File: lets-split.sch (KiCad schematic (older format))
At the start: 54 parts, among them J1 USB_C_Receptacle_USB2.0, SW1 Key_Tab, SW10 Key_D, SW11 Key_F, SW12 Key_G, SW13 Key_Shift, SW14 Key_Z, SW15 Key_X, SW16 Key_C, SW17 Key_V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

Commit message: Corrected footprint associations
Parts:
- D1, D10, D11, D12, D13, D14, D15, D16, D17, D18, D19, D2, D20, D21, D22, D23, D24, D3, D4, D5, D6, D7, D8, D9: footprint Diode_THT:D_DO-34_SOD68_P7.62mm_Horizontal -> Diode_THT:D_DO-35_SOD27_P7.62mm_Horizontal
- R1, R2, R3: footprint Resistor_THT:R_Axial_DIN0207_L6.3mm_D2.5mm_P10.16mm_Horizontal -> Resistor_THT:R_Axial_DIN0207_L6.3mm_D2.5mm_P7.62mm_Horizontal
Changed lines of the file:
@@
 F 0 "D1" V 1546 2070 50  0000 L CNN
 F 1 "D_Small" V 1455 2070 50  0000 L CNN
-F 2 "Diode_THT:D_DO-34_SOD68_P7.62mm_Horizontal" V 1500 2000 50  0001 C CNN
+F 2 "Diode_THT:D_DO-35_SOD27_P7.62mm_Horizontal" V 1500 2000 50  0001 C CNN
 F 3 "~" V 1500 2000 50  0001 C CNN
 	1    1500 2000
@@
 F 0 "D2" V 2346 2070 50  0000 L CNN
 F 1 "D_Small" V 2255 2070 50  0000 L CNN
-F 2 "Diode_THT:D_DO-34_SOD68_P7.62mm_Horizontal" V 2300 2000 50  0001 C CNN
+F 2 "Diode_THT:D_DO-35_SOD27_P7.62mm_Horizontal" V 2300 2000 50  0001 C CNN
 F 3 "~" V 2300 2000 50  0001 C CNN
 	1    2300 2000
@@
 F 0 "D3" V 3196 2070 50  0000 L CNN
 F 1 "D_Small" V 3105 2070 50  0000 L CNN
-F 2 "Diode_THT:D_DO-34_SOD68_P7.62mm_Horizontal" V 3150 2000 50  0001 C CNN
+F 2 "Diode_THT:D_DO-35_SOD27_P7.62mm_Horizontal" V 3150 2000 50  0001 C CNN
 F 3 "~" V 3150 2000 50  0001 C CNN
 	1    3150 2000
@@
 F 0 "D4" V 4046 2070 50  0000 L CNN
 F 1 "D_Small" V 3955 2070 50  0000 L CNN
-F 2 "Diode_THT:D_DO-34_SOD68_P7.62mm_Horizontal" V 4000 2000 50  0001 C CNN
+F 2 "Diode_THT:D_DO-35_SOD27_P7.62mm_Horizontal" V 4000 2000 50  0001 C CNN
 F 3 "~" V 4000 2000 50  0001 C CNN
 	1    4000 2000
@@
 F 0 "D5" V 4846 2070 50  0000 L CNN
 F 1 "D_Small" V 4755 2070 50  0000 L CNN
-F 2 "Diode_THT:D_DO-34_SOD68_P7.62mm_Horizontal" V 4800 2000 50  0001 C CNN
+F 2 "Diode_THT:D_DO-35_SOD27_P7.62mm_Horizontal" V 4800 2000 50  0001 C CNN
 F 3 "~" V 4800 2000 50  0001 C CNN
 	1    4800 2000
@@
 F 0 "D6" V 5746 2070 50  0000 L CNN
 F 1 "D_Small" V 5655 2070 50  0000 L CNN
-F 2 "Diode_THT:D_DO-34_SOD68_P7.62mm_Horizontal" V 5700 2000 50  0001 C CNN
+F 2 "Diode_THT:D_DO-35_SOD27_P7.62mm_Horizontal" V 5700 2000 50  0001 C CNN
 F 3 "~" V 5700 2000 50  0001 C CNN
 	1    5700 2000
@@
 F 0 "D7" V 1546 2670 50  0000 L CNN
 F 1 "D_Small" V 1455 2670 50  0000 L CNN
-F 2 "Diode_THT:D_DO-34_SOD68_P7.62mm_Horizontal" V 1500 2600 50  0001 C CNN
+F 2 "Diode_THT:D_DO-35_SOD27_P7.62mm_Horizontal" V 1500 2600 50  0001 C CNN
 F 3 "~" V 1500 2600 50  0001 C CNN
 	1    1500 2600
@@
 F 0 "D8" V 2346 2670 50  0000 L CNN
 F 1 "D_Small" V 2255 2670 50  0000 L CNN
-F 2 "Diode_THT:D_DO-34_SOD68_P7.62mm_Horizontal" V 2300 2600 50  0001 C CNN
+F 2 "Diode_THT:D_DO-35_SOD27_P7.62mm_Horizontal" V 2300 2600 50  0001 C CNN
 F 3 "~" V 2300 2600 50  0001 C CNN
 	1    2300 2600
@@
 F 0 "D9" V 3196 2670 50  0000 L CNN
 F 1 "D_Small" V 3105 2670 50  0000 L CNN
-F 2 "Diode_THT:D_DO-34_SOD68_P7.62mm_Horizontal" V 3150 2600 50  0001 C CNN
+F 2 "Diode_THT:D_DO-35_SOD27_P7.62mm_Horizontal" V 3150 2600 50  0001 C CNN
 F 3 "~" V 3150 2600 50  0001 C CNN
 	1    3150 2600
@@
 F 0 "D10" V 4046 2670 50  0000 L CNN
 F 1 "D_Small" V 3955 2670 50  0000 L CNN
-F 2 "Diode_THT:D_DO-34_SOD68_P7.62mm_Horizontal" V 4000 2600 50  0001 C CNN
+F 2 "Diode_THT:D_DO-35_SOD27_P7.62mm_Horizontal" V 4000 2600 50  0001 C CNN
 F 3 "~" V 4000 2600 50  0001 C CNN
 	1    4000 2600
@@
 F 0 "D11" V 4846 2670 50  0000 L CNN
 F 1 "D_Small" V 4755 2670 50  0000 L CNN
-F 2 "Diode_THT:D_DO-34_SOD68_P7.62mm_Horizontal" V 4800 2600 50  0001 C CNN
+F 2 "Diode_THT:D_DO-35_SOD27_P7.62mm_Horizontal" V 4800 2600 50  0001 C CNN
 F 3 "~" V 4800 2600 50  0001 C CNN
 	1    4800 2600
@@
 F 0 "D12" V 5746 2670 50  0000 L CNN
 F 1 "D_Small" V 5655 2670 50  0000 L CNN
-F 2 "Diode_THT:D_DO-34_SOD68_P7.62mm_Horizontal" V 5700 2600 50  0001 C CNN
+F 2 "Diode_THT:D_DO-35_SOD27_P7.62mm_Horizontal" V 5700 2600 50  0001 C CNN
 F 3 "~" V 5700 2600 50  0001 C CNN
 	1    5700 2600
@@
 F 0 "D13" V 1546 3270 50  0000 L CNN
 F 1 "D_Small" V 1455 3270 50  0000 L CNN
-F 2 "Diode_THT:D_DO-34_SOD68_P7.62mm_Horizontal" V 1500 3200 50  0001 C CNN
+F 2 "Diode_THT:D_DO-35_SOD27_P7.62mm_Horizontal" V 1500 3200 50  0001 C CNN
 F 3 "~" V 1500 3200 50  0001 C CNN
 	1    1500 3200
@@
 F 0 "D14" V 2346 3270 50  0000 L CNN
 F 1 "D_Small" V 2255 3270 50  0000 L CNN
-F 2 "Diode_THT:D_DO-34_SOD68_P7.62mm_Horizontal" V 2300 3200 50  0001 C CNN
+F 2 "Diode_THT:D_DO-35_SOD27_P7.62mm_Horizontal" V 2300 3200 50  0001 C CNN
 F 3 "~" V 2300 3200 50  0001 C CNN
 	1    2300 3200
@@
 F 0 "D15" V 3196 3270 50  0000 L CNN
 F 1 "D_Small" V 3105 3270 50  0000 L CNN
-F 2 "Diode_THT:D_DO-34_SOD68_P7.62mm_Horizontal" V 3150 3200 50  0001 C CNN
+F 2 "Diode_THT:D_DO-35_SOD27_P7.62mm_Horizontal" V 3150 3200 50  0001 C CNN
 F 3 "~" V 3150 3200 50  0001 C CNN
 	1    3150 3200
@@
 F 0 "D16" V 4046 3270 50  0000 L CNN
 F 1 "D_Small" V 3955 3270 50  0000 L CNN
-F 2 "Diode_THT:D_DO-34_SOD68_P7.62mm_Horizontal" V 4000 3200 50  0001 C CNN
+F 2 "Diode_THT:D_DO-35_SOD27_P7.62mm_Horizontal" V 4000 3200 50  0001 C CNN
 F 3 "~" V 4000 3200 50  0001 C CNN
 	1    4000 3200
@@
 F 0 "D17" V 4846 3270 50  0000 L CNN
 F 1 "D_Small" V 4755 3270 50  0000 L CNN
-F 2 "Diode_THT:D_DO-34_SOD68_P7.62mm_Horizontal" V 4800 3200 50  0001 C CNN
+F 2 "Diode_THT:D_DO-35_SOD27_P7.62mm_Horizontal" V 4800 3200 50  0001 C CNN
 F 3 "~" V 4800 3200 50  0001 C CNN
 	1    4800 3200
@@
 F 0 "D18" V 5746 3270 50  0000 L CNN
 F 1 "D_Small" V 5655 3270 50  0000 L CNN
-F 2 "Diode_THT:D_DO-34_SOD68_P7.62mm_Horizontal" V 5700 3200 50  0001 C CNN
+F 2 "Diode_THT:D_DO-35_SOD27_P7.62mm_Horizontal" V 5700 3200 50  0001 C CNN
 F 3 "~" V 5700 3200 50  0001 C CNN
 	1    5700 3200
@@
 F 0 "D19" V 1546 3870 50  0000 L CNN
 F 1 "D_Small" V 1455 3870 50  0000 L CNN
-F 2 "Diode_THT:D_DO-34_SOD68_P7.62mm_Horizontal" V 1500 3800 50  0001 C CNN
+F 2 "Diode_THT:D_DO-35_SOD27_P7.62mm_Horizontal" V 1500 3800 50  0001 C CNN
 F 3 "~" V 1500 3800 50  0001 C CNN
 	1    1500 3800
@@
 F 0 "D20" V 2346 3870 50  0000 L CNN
 F 1 "D_Small" V 2255 3870 50  0000 L CNN
-F 2 "Diode_THT:D_DO-34_SOD68_P7.62mm_Horizontal" V 2300 3800 50  0001 C CNN
+F 2 "Diode_THT:D_DO-35_SOD27_P7.62mm_Horizontal" V 2300 3800 50  0001 C CNN
 F 3 "~" V 2300 3800 50  0001 C CNN
 	1    2300 3800
@@
 F 0 "D21" V 3196 3870 50  0000 L CNN
 F 1 "D_Small" V 3105 3870 50  0000 L CNN
-F 2 "Diode_THT:D_DO-34_SOD68_P7.62mm_Horizontal" V 3150 3800 50  0001 C CNN
+F 2 "Diode_THT:D_DO-35_SOD27_P7.62mm_Horizontal" V 3150 3800 50  0001 C CNN
 F 3 "~" V 3150 3800 50  0001 C CNN
 	1    3150 3800
@@
 F 0 "D22" V 4046 3870 50  0000 L CNN
 F 1 "D_Small" V 3955 3870 50  0000 L CNN
-F 2 "Diode_THT:D_DO-34_SOD68_P7.62mm_Horizontal" V 4000 3800 50  0001 C CNN
+F 2 "Diode_THT:D_DO-35_SOD27_P7.62mm_Horizontal" V 4000 3800 50  0001 C CNN
 F 3 "~" V 4000 3800 50  0001 C CNN
 	1    4000 3800
@@
 F 0 "D23" V 4846 3870 50  0000 L CNN
 F 1 "D_Small" V 4755 3870 50  0000 L CNN
-F 2 "Diode_THT:D_DO-34_SOD68_P7.62mm_Horizontal" V 4800 3800 50  0001 C CNN
+F 2 "Diode_THT:D_DO-35_SOD27_P7.62mm_Horizontal" V 4800 3800 50  0001 C CNN
 F 3 "~" V 4800 3800 50  0001 C CNN
 	1    4800 3800
@@
 F 0 "D24" V 5746 3870 50  0000 L CNN
 F 1 "D_Small" V 5655 3870 50  0000 L CNN
-F 2 "Diode_THT:D_DO-34_SOD68_P7.62mm_Horizontal" V 5700 3800 50  0001 C CNN
+F 2 "Diode_THT:D_DO-35_SOD27_P7.62mm_Horizontal" V 5700 3800 50  0001 C CNN
 F 3 "~" V 5700 3800 50  0001 C CNN
 	1    5700 3800
@@
 F 0 "R3" H 8309 5396 50  0000 L CNN
 F 1 "220" H 8309 5305 50  0000 L CNN
-F 2 "Resistor_THT:R_Axial_DIN0207_L6.3mm_D2.5mm_P10.16mm_Horizontal" H 8250 5350 50  0001 C CNN
+F 2 "Resistor_THT:R_Axial_DIN0207_L6.3mm_D2.5mm_P7.62mm_Horizontal" H 8250 5350 50  0001 C CNN
 F 3 "~" H 8250 5350 50  0001 C CNN
 	1    8250 5350
@@
 F 0 "R2" H 9109 2696 50  0000 L CNN
 F 1 "9.1k" H 9109 2605 50  0000 L CNN
-F 2 "Resistor_THT:R_Axial_DIN0207_L6.3mm_D2.5mm_P10.16mm_Horizontal" H 9050 2650 50  0001 C CNN
+F 2 "Resistor_THT:R_Axial_DIN0207_L6.3mm_D2.5mm_P7.62mm_Horizontal" H 9050 2650 50  0001 C CNN
 F 3 "~" H 9050 2650 50  0001 C CNN
 	1    9050 2650
@@
 F 0 "R1" H 9109 2296 50  0000 L CNN
 F 1 "9.1k" H 9109 2205 50  0000 L CNN
-F 2 "Resistor_THT:R_Axial_DIN0207_L6.3mm_D2.5mm_P10.16mm_Horizontal" H 9050 2250 50  0001 C CNN
+F 2 "Resistor_THT:R_Axial_DIN0207_L6.3mm_D2.5mm_P7.62mm_Horizontal" H 9050 2250 50  0001 C CNN
 F 3 "~" H 9050 2250 50  0001 C CNN
 	1    9050 2250

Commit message: corrected reset button footprint
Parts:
- SW25: footprint keyswitches:SW_MX_reversible -> Button_Switch_THT:SW_PUSH_6mm_H4.3mm
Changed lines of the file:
@@
 F 0 "SW25" H 5650 6535 50  0000 C CNN
 F 1 "Reset" H 5650 6444 50  0000 C CNN
-F 2 "keyswitches:SW_MX_reversible" H 5650 6450 50  0001 C CNN
+F 2 "Button_Switch_THT:SW_PUSH_6mm_H4.3mm" H 5650 6450 50  0001 C CNN
 F 3 "~" H 5650 6450 50  0001 C CNN
 	1    5650 6250

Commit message: Fixed USB-C connector not passing inspection.
Added jumper to allow it to be mounted on either side of the board
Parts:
- added JP1: Jack Reversed Jumper, Jumper:SolderJumper-3_P1.3mm_Open_RoundedPad1.0x1.5mm, symbol Jumper:SolderJumper_3_Open
- added JP2: Jack Obversed Jumper, Jumper:SolderJumper-3_P1.3mm_Open_RoundedPad1.0x1.5mm, symbol Jumper:SolderJumper_3_Open
- J1: footprint Connector_USB:USB_C_Receptacle_GCT_USB4085 -> custom-footprints:USB_C_GCT_USB4085
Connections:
- net at J1.A5 (CC1): now also JP1.3 (B)
- net at J1.B5 (CC2): now also JP1.2 (C)
- new net: J1.A8 (SBU1), JP2.2 (C)
- new net: J1.B8 (SBU2), JP2.1 (A)
- new net: JP1.1 (A), JP2.3 (B), R3.1
- no-connect marks 6 -> 11
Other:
- moved on the sheet: R3
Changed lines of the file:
@@
 F 0 "J1" H 8620 4789 50  0000 R CNN
 F 1 "USB_C_Receptacle_USB2.0" H 8620 4698 50  0000 R CNN
-F 2 "Connector_USB:USB_C_Receptacle_GCT_USB4085" H 9200 4850 50  0001 C CNN
+F 2 "custom-footprints:USB_C_GCT_USB4085" H 9200 4850 50  0001 C CNN
 F 3 "https://www.usb.org/sites/default/files/documents/usb_type-c.zip" H 9200 4850 50  0001 C CNN
 	1    9050 4850
@@
 Text GLabel 2150 5950 0    50   Input ~ 0
 Serial1
-Text GLabel 8050 5350 0    50   Input ~ 0
+Text GLabel 7500 4950 0    50   Input ~ 0
 Serial1
-Wire Wire Line
-	8350 5350 8450 5350
-Wire Wire Line
-	8450 5450 8450 5350
-Connection ~ 8450 5350
 $Comp
 L power:VCC #PWR03
@@
 L Device:R_Small R3
 U 1 1 60DE63E5
-P 8250 5350
-F 0 "R3" H 8309 5396 50  0000 L CNN
-F 1 "220" H 8309 5305 50  0000 L CNN
-F 2 "Resistor_THT:R_Axial_DIN0207_L6.3mm_D2.5mm_P7.62mm_Horizontal" H 8250 5350 50  0001 C CNN
-F 3 "~" H 8250 5350 50  0001 C CNN
-	1    8250 5350
+P 7700 4950
+F 0 "R3" H 7759 4996 50  0000 L CNN
+F 1 "220" H 7759 4905 50  0000 L CNN
+F 2 "Resistor_THT:R_Axial_DIN0207_L6.3mm_D2.5mm_P7.62mm_Horizontal" H 7700 4950 50  0001 C CNN
+F 3 "~" H 7700 4950 50  0001 C CNN
+	1    7700 4950
 	0    1    1    0
 $EndComp
-NoConn ~ 8450 4550
-NoConn ~ 8450 4450
 NoConn ~ 8450 4750
 NoConn ~ 8450 4850
@@
 Comms
 Wire Wire Line
-	8050 5350 8150 5350
+	7500 4950 7600 4950
 Wire Wire Line
 	9050 5850 9050 5750
@@
 Text Notes 5200 5550 0    118  ~ 0
 Reset Button
+NoConn ~ 2150 5850
+NoConn ~ 2150 6250
+NoConn ~ 2150 6350
+NoConn ~ 2150 6450
+NoConn ~ 2150 6550
+NoConn ~ 3550 6250
+NoConn ~ 3550 5850
+$Comp
+L Jumper:SolderJumper_3_Open JP1
+U 1 1 60EF25DC
+P 8000 4450
+F 0 "JP1" H 8000 4655 50  0000 C CNN
+F 1 "Jack Reversed Jumper" H 8000 4564 50  0000 C CNN
+F 2 "Jumper:SolderJumper-3_P1.3mm_Open_RoundedPad1.0x1.5mm" H 8000 4450 50  0001 C CNN
+F 3 "~" H 8000 4450 50  0001 C CNN
+	1    8000 4450
+	1    0    0    -1
+$EndComp
+$Comp
+L Jumper:SolderJumper_3_Open JP2
+U 1 1 60EF4046
+P 8000 5450
+F 0 "JP2" H 8000 5563 50  0000 C CNN
+F 1 "Jack Obversed Jumper" H 8000 5654 50  0000 C CNN
+F 2 "Jumper:SolderJumper-3_P1.3mm_Open_RoundedPad1.0x1.5mm" H 8000 5450 50  0001 C CNN
+F 3 "~" H 8000 5450 50  0001 C CNN
+	1    8000 5450
+	-1   0    0    1
+$EndComp
+Wire Wire Line
+	7800 5450 7800 4950
+Wire Wire Line
+	7800 4950 7800 4450
+Connection ~ 7800 4950
+Wire Wire Line
+	8000 4600 8450 4600
+Wire Wire Line
+	8450 4600 8450 4550
+Wire Wire Line
+	8450 4450 8200 4450
+Wire Wire Line
+	8450 5450 8200 5450
+Wire Wire Line
+	8450 5350 8450 5300
+Wire Wire Line
+	8450 5300 8000 5300
 $EndSCHEMATC

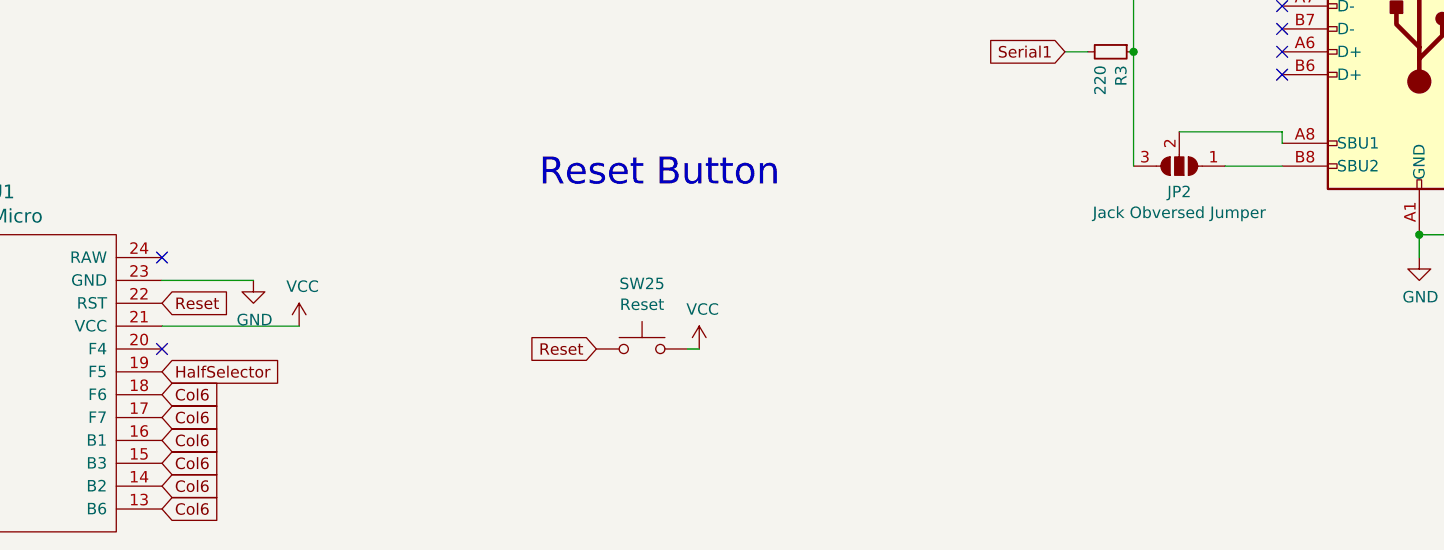
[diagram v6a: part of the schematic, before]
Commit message: PCB traces laid. Fixed labels on columns on schematic.
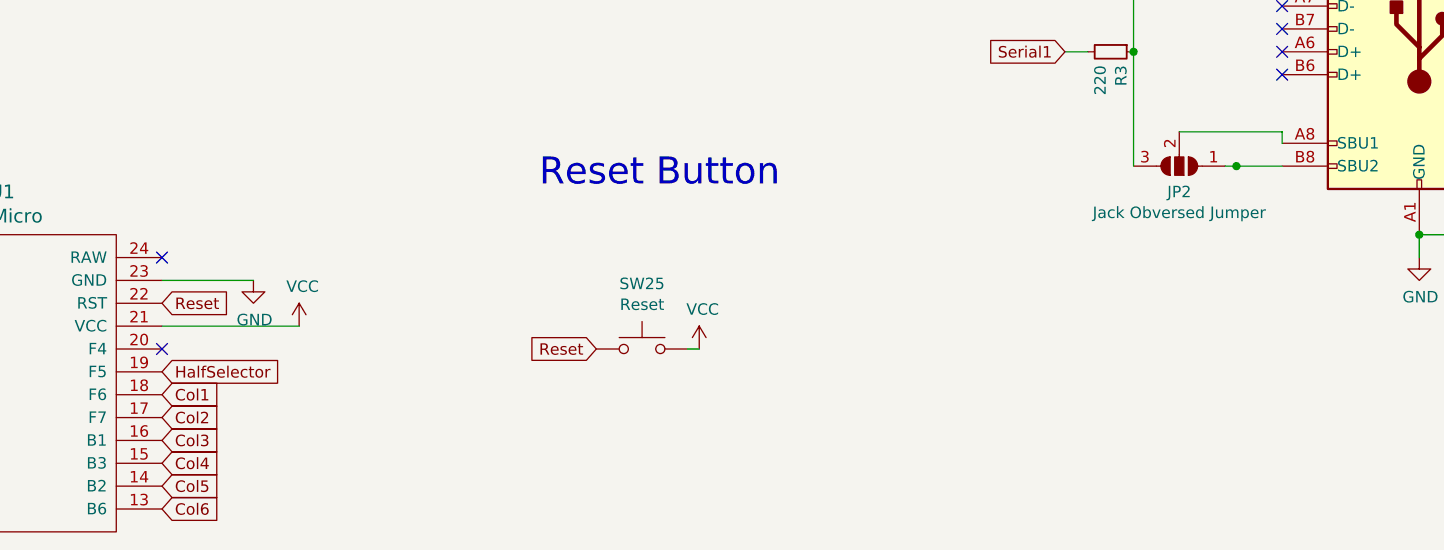
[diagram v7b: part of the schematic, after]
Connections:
- net Col1: now also U1.18 (F6)
- net Col2: now also U1.17 (F7)
- net Col3: now also U1.16 (B1)
- net Col4: now also U1.15 (B3)
- net Col5: now also U1.14 (B2)
- net Col6: no longer U1.14 (B2), U1.15 (B3), U1.16 (B1), U1.17 (F7), U1.18 (F6)
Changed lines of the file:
@@
 Col6
 Text GLabel 3550 6850 2    50   Input ~ 0
-Col6
+Col5
 Text GLabel 3550 6750 2    50   Input ~ 0
-Col6
+Col4
 Text GLabel 3550 6650 2    50   Input ~ 0
-Col6
+Col3
 Text GLabel 3550 6550 2    50   Input ~ 0
-Col6
+Col2
 Text GLabel 3550 6450 2    50   Input ~ 0
-Col6
+Col1
 $Comp
 L power:GND #PWR02
@@
 	8450 4450 8200 4450
 Wire Wire Line
-	8450 5450 8200 5450
+	8450 5450 8250 5450
 Wire Wire Line
 	8450 5350 8450 5300
 Wire Wire Line
 	8450 5300 8000 5300
+Connection ~ 8250 5450
+Wire Wire Line
+	8250 5450 8200 5450
 $EndSCHEMATC

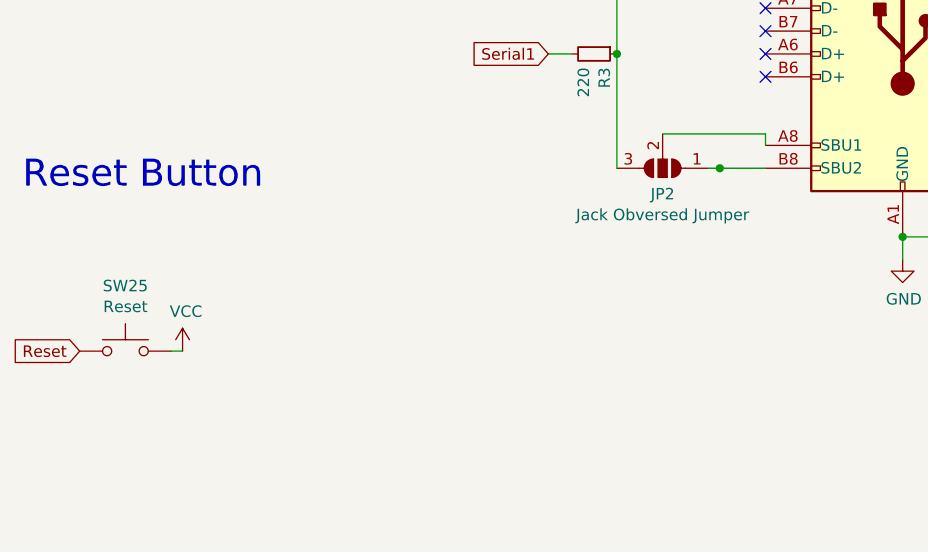
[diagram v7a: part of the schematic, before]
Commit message: corrected reset button to go to gnd
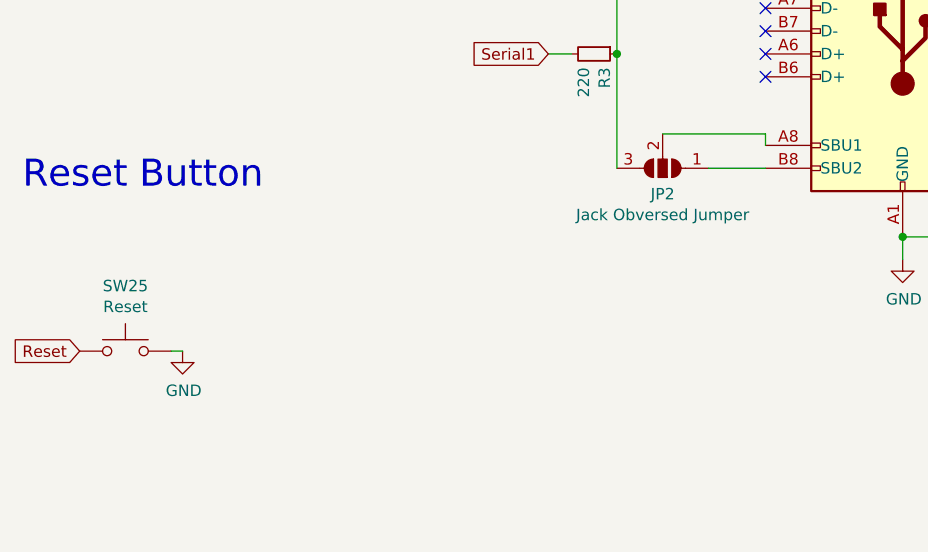
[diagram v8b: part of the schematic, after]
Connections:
- net GND: now also SW25.2
- net VCC: no longer SW25.2
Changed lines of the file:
@@
 Text GLabel 5450 6250 0    50   Input ~ 0
 Reset
-$Comp
-L power:VCC #PWR08
-U 1 1 60E6443B
-P 5900 6250
-F 0 "#PWR08" H 5900 6100 50  0001 C CNN
-F 1 "VCC" H 5915 6423 50  0000 C CNN
-F 2 "" H 5900 6250 50  0001 C CNN
-F 3 "" H 5900 6250 50  0001 C CNN
-	1    5900 6250
-	1    0    0    -1
-$EndComp
 Wire Wire Line
 	5900 6250 5850 6250
@@
 	8450 4450 8200 4450
 Wire Wire Line
-	8450 5450 8250 5450
-Wire Wire Line
 	8450 5350 8450 5300
 Wire Wire Line
 	8450 5300 8000 5300
-Connection ~ 8250 5450
 Wire Wire Line
-	8250 5450 8200 5450
+	8200 5450 8450 5450
+$Comp
+L power:GND #PWR?
+U 1 1 60C67E49
+P 5900 6250
+F 0 "#PWR?" H 5900 6000 50  0001 C CNN
+F 1 "GND" H 5905 6077 50  0000 C CNN
+F 2 "" H 5900 6250 50  0001 C CNN
+F 3 "" H 5900 6250 50  0001 C CNN
+	1    5900 6250
+	1    0    0    -1
+$EndComp
 $EndSCHEMATC
